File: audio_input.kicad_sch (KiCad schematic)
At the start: 12 parts

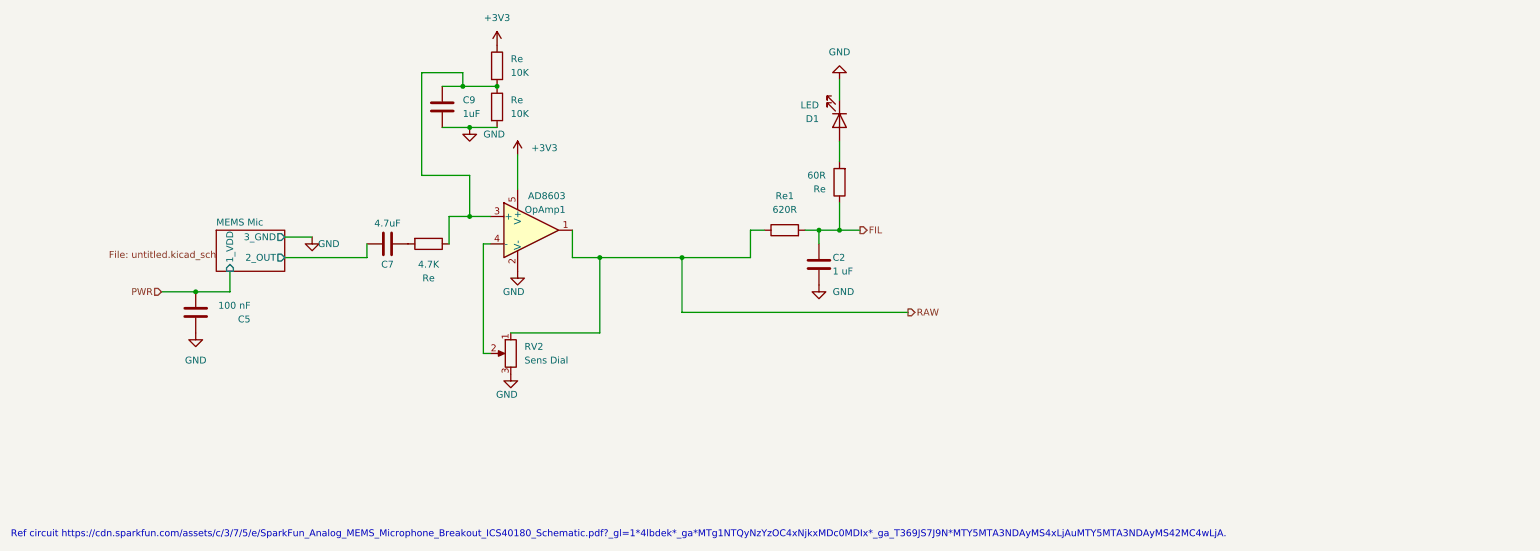
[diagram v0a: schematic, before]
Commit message: new pcb rev with updated audio filter
The only ERC and DRC warnings/errors are unconnected pins and silkscreen text issues. There are two DRC issues that have to do with the mic, but I don't think they're an issue
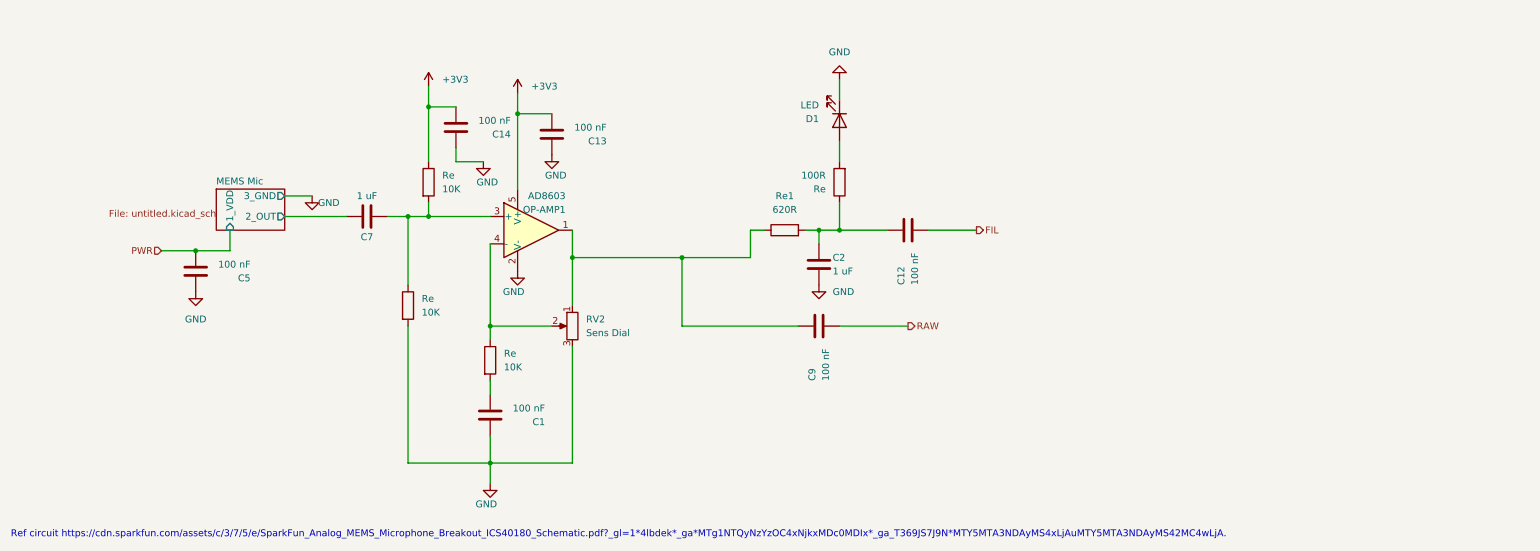
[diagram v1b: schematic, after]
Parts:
- removed Re (x2): 10K, Resistor_SMD:R_0603_1608Metric_Pad0.98x0.95mm_HandSolder, symbol Device:R
- added C1, C12, C13, C14: 100 nF, Capacitor_SMD:C_0603_1608Metric_Pad1.08x0.95mm_HandSolder, symbol Device:C
- added Re (x2): 10K, Resistor_SMD:R_0603_1608Metric_Pad0.98x0.95mm_HandSolder, symbol Device:R
- C7: value 4.7uF -> 1 uF
- C9: value 1uF -> 100 nF
- Re: value 60R -> 100R
- Re: value 4.7K -> 10K
- renumbered OpAmp1 to OP-AMP1
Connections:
- net +3V3: now also C13.2, C14.2, Re.1
- net FIL: now also C12.2; no longer C2.2, Re.1, Re1.2
- net GND: now also Re.2, C1.1, C13.1, C14.1; no longer C9.1
- net RAW: now also C9.2; no longer OP-AMP1.1, RV2.1, Re1.1
- net at OP-AMP1.3 (+), Re.1: now also C7.1, Re.2; no longer C9.2
- net at OP-AMP1.4 (-), RV2.2: now also Re.1
- new net: C1.2, Re.2
- new net: C12.1, C2.2, Re.1, Re1.2
- new net: C9.1, OP-AMP1.1, RV2.1, Re1.1
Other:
- moved on the sheet: C5, C7, RV2, Re
